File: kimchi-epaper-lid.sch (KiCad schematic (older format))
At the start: 8 parts, among them J1 DF40HC(3.5)-60DS, J2 DF40HC(3.5)-60DS, U1 24C32

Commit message: Partially completed schematics of the lid
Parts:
- added C1, C2, C3, C4, C5, C6, C7, C8, C9: 1uF, symbol Device:C_Small
- added C10, R1, R2: 0.1uF, symbol Device:C_Small
- added IC1: TXS0104ED, SOIC127P600X175-14N, symbol TXS0104ED:TXS0104ED
- added R3, R4: 10k, symbol Device:R_Small_US
- added X1: 52435-2471, symbol epaper-fpc-connector:52435-2471
- renumbered H3 to H2, H2 to H3
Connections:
- net ECSPI1_MOSI: now also X1.14 (D1_Data)
- net ECSPI1_SCLK: now also X1.13 (D0_Clock)
- net ECSPI1_SS0: now also X1.12 (CS)
- net GND: now also C1.2, C10.1, C2.1, C3.1, C4.2, C5.2, C6.2, C7.1, C8.2, C9.1, IC1.7 (GND), R1.1, R2.1, R3.2, R4.2, X1.17 (VSS), X1.8 (BS1)
- net VDD_1V8: now also IC1.1 (VCCA), R1.2
- net VDD_3V3: now also IC1.14 (VCCB), R2.2
- new net: IC1.8 (OE), R3.1
- new net: C3.2, X1.18 (VDD)
- new net: C4.1, X1.19 (VPP)
- new net: C5.1, X1.20 (VSH)
- new net: C6.1, X1.22 (VSL)
- new net: C7.2, X1.24 (VCOM)
- new net: C8.1, X1.4 (VGL)
- new net: C9.2, X1.5 (VGH)
- new net +3V3: C10.2, X1.15 (VDDIO), X1.16 (VCI)
- new net GDR: R4.1, X1.2 (GDR)
- new net LC_BUSY: IC1.13 (B1), X1.9 (BUSY)
- new net LC_DC: IC1.11 (B3), X1.11 (D/C)
- new net LC_RST: IC1.12 (B2), X1.10 (RST)
- new net PREVGH: C1.1, X1.21 (PREVGH)
- new net PREVGL: C2.2, X1.23 (PREVGL)
- new net RESE: X1.3 (RESE)
- no-connect marks 0 -> 7
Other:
- note added: "EINK Display Section"
- note added: "Level Convertor\n"
- note added: "Place close to the connector\n"

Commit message: prouting a few components and updated position
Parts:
- removed IC1: TXS0104ED, SOIC127P600X175-14N, symbol TXS0104ED:TXS0104ED
- removed R1, R2: 0.1uF, symbol Device:C_Small
- removed R3: 10k, symbol Device:R_Small_US
- added C1: 2.2uF, Capacitor_SMD:C_0603_1608Metric, symbol Device:C_Small
- added C2: 1uF, Capacitor_SMD:C_0603_1608Metric, symbol Device:C_Small
- added D1, D2, D3: MBR0530T3G, Diode_SMD:D_SOD-123, symbol Diode:MBR0530
- added L1: 68uH, NLV32T-680J-EF:INDM3225X240N, symbol Device:L_Core_Iron
- added Q1: SI1308EDL-T1-BE3, SI1308EDL-T1-BE3:SOT65P210X110-3N, symbol SI1308EDL-T1-BE3:SI1308EDL-T1-BE3
- added R2: 2.2k, Resistor_SMD:R_0603_1608Metric, symbol Device:R_Small_US
- C10: renamed from C8; footprint (none) -> Capacitor_SMD:C_0603_1608Metric
- C11: renamed from C9; footprint (none) -> Capacitor_SMD:C_0603_1608Metric
- C12: renamed from C10; footprint (none) -> Capacitor_SMD:C_0603_1608Metric
- C3: renamed from C1; footprint (none) -> Capacitor_SMD:C_0603_1608Metric
- C4: renamed from C2; footprint (none) -> Capacitor_SMD:C_0603_1608Metric
- C5: renamed from C3; footprint (none) -> Capacitor_SMD:C_0603_1608Metric
- C6: renamed from C4; footprint (none) -> Capacitor_SMD:C_0603_1608Metric
- C7: renamed from C5; footprint (none) -> Capacitor_SMD:C_0603_1608Metric
- C8: renamed from C6; footprint (none) -> Capacitor_SMD:C_0603_1608Metric
- C9: renamed from C7; footprint (none) -> Capacitor_SMD:C_0603_1608Metric
- R1: renamed from R4; footprint (none) -> Resistor_SMD:R_0603_1608Metric
- X1: footprint (none) -> epaper-fpc-connector:MOLEX_52435-2471
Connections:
- net +3V3 is gone; now on net VDD_3V3: C12.2, X1.15 (VDDIO), X1.16 (VCI)
- net LC_BUSY is gone; now on net SAI3_MCLK: X1.9 (BUSY)
- net LC_DC is gone; now on net SAI3_RXC: X1.11 (D/C)
- net LC_RST is gone; now on net SAI3_TXFS: X1.10 (RST)
- net GDR: now also Q1.1
- net GND: now also C1.2, D1.1 (K), R2.2
- net PREVGH: now also D3.1 (K)
- net PREVGL: now also D2.2 (A)
- net RESE: now also Q1.3, R2.1
- net VDD_3V3: now also C1.1, L1.1
- new net: C2.1, D1.2 (A), D2.1 (K)
- new net: C2.2, D3.2 (A), L1.2, Q1.2
- no-connect marks 7 -> 3
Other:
- note removed: "Level Convertor\n"
- moved on the sheet: C10, C11, C12, C3, C4, C5, C6, C7, C8, C9, R1, X1

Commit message: Fixed issues with routing
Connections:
- net USB2_DN is gone; now on net PCIE_USB_D_N: J1.59 (Pin_59)
- net USB2_DP is gone; now on net PCIE_USB_D_P: J1.60 (Pin_60)
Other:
- note added: "Connected these together, so that USB2 pins \nwill be accessible on the PCIE port, as they \nare not being used."
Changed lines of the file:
@@
 	1    0    0    -1
 $EndComp
+Text GLabel 12010 2540 3    50   Input ~ 0
+PCIE_USB_D_N
+Text GLabel 12430 2540 3    50   Input ~ 0
+PCIE_USB_D_P
+Text GLabel 12430 1935 1    50   Input ~ 0
+USB2_DP
+Text GLabel 12010 1940 1    50   Input ~ 0
+USB2_DN
+Wire Wire Line
+	12010 2540 12010 1940
+Wire Wire Line
+	12430 1935 12430 2540
+Text Notes 12565 2435 0    79   ~ 0
+Connected these together, so that USB2 pins \nwill be accessible on the PCIE port, as they \nare not being used.
 $EndSCHEMATC

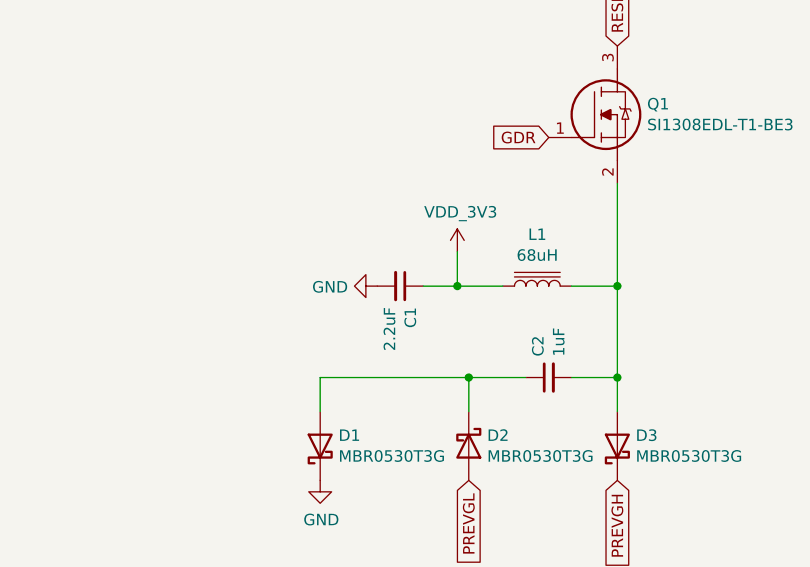
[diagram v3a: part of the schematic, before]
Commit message: Replaced inductor and completed routing (acq review)
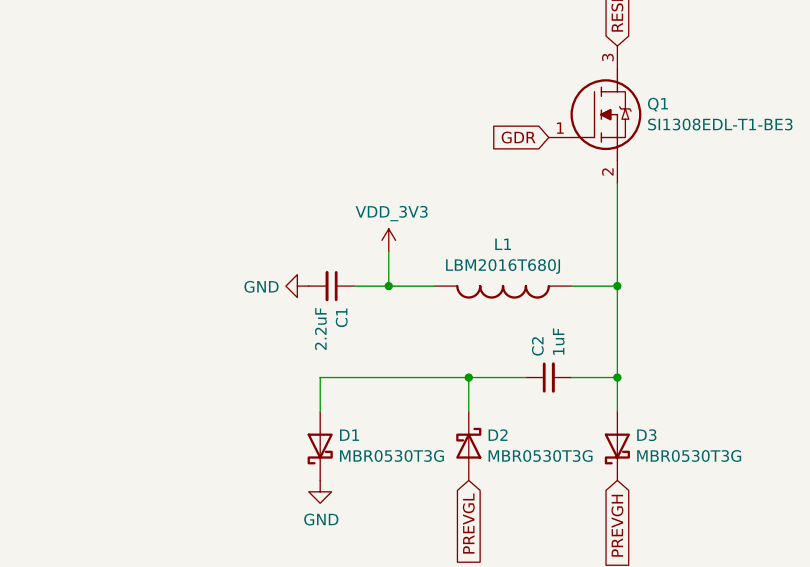
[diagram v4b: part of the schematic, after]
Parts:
- removed L1: 68uH, NLV32T-680J-EF:INDM3225X240N, symbol Device:L_Core_Iron
- added L1: LBM2016T680J, LBM2016T680J:INDC2016X180N, symbol LBM2016T680J:LBM2016T680J
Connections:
- net VDD_3V3: now also L1.1
- net at C2.2, D3.2 (A), Q1.2: now also L1.2
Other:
- moved on the sheet: C1
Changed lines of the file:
@@
 L Device:C_Small C1
 U 1 1 6029C582
-P 4400 7700
-F 0 "C1" H 4308 7746 50  0000 R CNN
-F 1 "2.2uF" H 4308 7655 50  0000 R CNN
-F 2 "Capacitor_SMD:C_0603_1608Metric" H 4400 7700 50  0001 C CNN
-F 3 "~" H 4400 7700 50  0001 C CNN
-	1    4400 7700
+P 4100 7700
+F 0 "C1" H 4008 7746 50  0000 R CNN
+F 1 "2.2uF" H 4008 7655 50  0000 R CNN
+F 2 "Capacitor_SMD:C_0603_1608Metric" H 4100 7700 50  0001 C CNN
+F 3 "~" H 4100 7700 50  0001 C CNN
+	1    4100 7700
 	0    1    -1   0
 $EndComp
@@
 	1    5050 8100
 	0    -1   1    0
-$EndComp
-$Comp
-L Device:L_Core_Iron L1
-U 1 1 6029F5E3
-P 5000 7700
-F 0 "L1" V 5225 7700 50  0000 C CNN
-F 1 "68uH" V 5134 7700 50  0000 C CNN
-F 2 "NLV32T-680J-EF:INDM3225X240N" H 5000 7700 50  0001 C CNN
-F 3 "~" H 5000 7700 50  0001 C CNN
-	1    5000 7700
-	0    -1   -1   0
 $EndComp
 $Comp
@@
 	5350 7700 5350 8100
 Wire Wire Line
-	4850 7700 4650 7700
+	4550 7700 4350 7700
 $Comp
 L power:GND #PWR06
 U 1 1 60330ACC
-P 4300 7700
-F 0 "#PWR06" H 4300 7450 50  0001 C CNN
-F 1 "GND" V 4305 7572 50  0000 R CNN
-F 2 "" H 4300 7700 50  0001 C CNN
-F 3 "" H 4300 7700 50  0001 C CNN
-	1    4300 7700
+P 4000 7700
+F 0 "#PWR06" H 4000 7450 50  0001 C CNN
+F 1 "GND" V 4005 7572 50  0000 R CNN
+F 2 "" H 4000 7700 50  0001 C CNN
+F 3 "" H 4000 7700 50  0001 C CNN
+	1    4000 7700
 	0    1    1    0
 $EndComp
 Wire Wire Line
-	4650 7550 4650 7700
-Connection ~ 4650 7700
+	4350 7550 4350 7700
+Connection ~ 4350 7700
 Wire Wire Line
-	4650 7700 4500 7700
+	4350 7700 4200 7700
 $Comp
 L power:GND #PWR05
@@
 RESE
 $Comp
-L kimchi_ulid:VDD_3V3 #PWR?
+L kimchi_ulid:VDD_3V3 #PWR014
 U 1 1 6048F43C
 P 9850 7600
-F 0 "#PWR?" H 9850 7450 50  0001 C CNN
+F 0 "#PWR014" H 9850 7450 50  0001 C CNN
 F 1 "VDD_3V3" V 9865 7727 50  0000 L CNN
 F 2 "" H 9850 7600 50  0001 C CNN
@@
 $EndComp
 $Comp
-L kimchi_ulid:VDD_3V3 #PWR?
+L kimchi_ulid:VDD_3V3 #PWR07
 U 1 1 604938CB
-P 4650 7550
-F 0 "#PWR?" H 4650 7400 50  0001 C CNN
-F 1 "VDD_3V3" H 4665 7723 50  0000 C CNN
-F 2 "" H 4650 7550 50  0001 C CNN
-F 3 "" H 4650 7550 50  0001 C CNN
-	1    4650 7550
+P 4350 7550
+F 0 "#PWR07" H 4350 7400 50  0001 C CNN
+F 1 "VDD_3V3" H 4365 7723 50  0000 C CNN
+F 2 "" H 4350 7550 50  0001 C CNN
+F 3 "" H 4350 7550 50  0001 C CNN
+	1    4350 7550
 	1    0    0    -1
 $EndComp
@@
 Text Notes 12565 2435 0    79   ~ 0
 Connected these together, so that USB2 pins \nwill be accessible on the PCIE port, as they \nare not being used.
+$Comp
+L LBM2016T680J:LBM2016T680J L1
+U 1 1 6068AC33
+P 4850 7700
+F 0 "L1" H 4850 7881 50  0000 C CNN
+F 1 "LBM2016T680J" H 4850 7790 50  0000 C CNN
+F 2 "LBM2016T680J:INDC2016X180N" H 4850 7700 50  0001 L BNN
+F 3 "" H 4850 7700 50  0001 L BNN
+	1    4850 7700
+	1    0    0    -1
+$EndComp
 $EndSCHEMATC

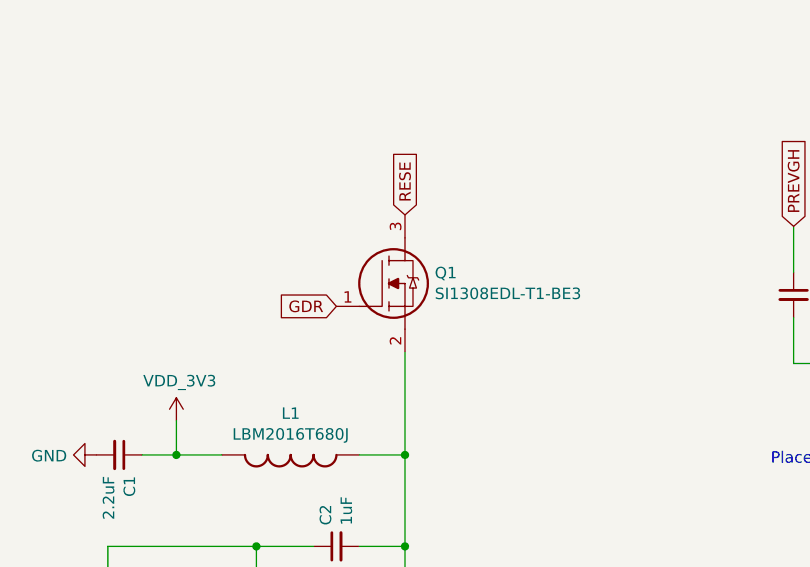
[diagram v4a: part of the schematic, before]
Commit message: Fixed mistake in mosfet schematics
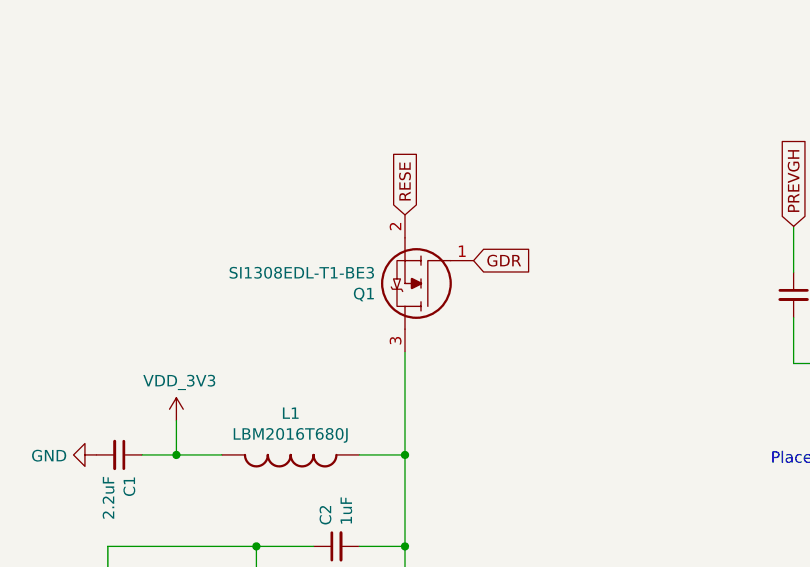
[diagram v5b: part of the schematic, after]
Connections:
- net RESE: now also Q1.2; no longer Q1.3
- net at C2.2, D3.2 (A), L1.2: now also Q1.3; no longer Q1.2
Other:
- moved on the sheet: Q1
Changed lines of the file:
@@
 	0    -1   1    0
-$EndComp
-$Comp
-L SI1308EDL-T1-BE3:SI1308EDL-T1-BE3 Q1
-U 1 1 602E5C48
-P 5050 7050
-F 0 "Q1" H 5480 7196 50  0000 L CNN
-F 1 "SI1308EDL-T1-BE3" H 5480 7105 50  0000 L CNN
-F 2 "SI1308EDL-T1-BE3:SOT65P210X110-3N" H 5500 7000 50  0001 L CNN
-F 3 "https://www.mouser.es/datasheet/2/427/si1308edl-1764588.pdf" H 5500 6900 50  0001 L CNN
-F 4 "MOSFET 30V N-CHANNEL (D-S)" H 5500 6800 50  0001 L CNN "Description"
-F 5 "1.1" H 5500 6700 50  0001 L CNN "Height"
-F 6 "Vishay" H 5500 6600 50  0001 L CNN "Manufacturer_Name"
-F 7 "SI1308EDL-T1-BE3" H 5500 6500 50  0001 L CNN "Manufacturer_Part_Number"
-F 8 "78-SI1308EDL-T1-BE3" H 5500 6400 50  0001 L CNN "Mouser Part Number"
-F 9 "https://www.mouser.co.uk/ProductDetail/Vishay-Siliconix/SI1308EDL-T1-BE3/?qs=zW32dvEIR3shhEGZ2ACCcQ%3D%3D" H 5500 6300 50  0001 L CNN "Mouser Price/Stock"
-F 10 "" H 5500 6200 50  0001 L CNN "Arrow Part Number"
-F 11 "" H 5500 6100 50  0001 L CNN "Arrow Price/Stock"
-	1    5050 7050
-	1    0    0    -1
 $EndComp
 Wire Wire Line
@@
 Text GLabel 5350 8550 3    50   Input ~ 0
 PREVGH
-Text GLabel 5050 7050 0    50   Input ~ 0
+Text GLabel 5650 6850 2    50   Input ~ 0
 GDR
 Text GLabel 5350 6650 1    50   Input ~ 0
@@
 	1    0    0    -1
 $EndComp
+$Comp
+L SI1308EDL-T1-BE3:SI1308EDL-T1-BE3 Q1
+U 1 1 602E5C48
+P 5650 6850
+F 0 "Q1" H 6080 6996 50  0000 L CNN
+F 1 "SI1308EDL-T1-BE3" H 6080 6905 50  0000 L CNN
+F 2 "SI1308EDL-T1-BE3:SOT65P210X110-3N" H 6100 6800 50  0001 L CNN
+F 3 "https://www.mouser.es/datasheet/2/427/si1308edl-1764588.pdf" H 6100 6700 50  0001 L CNN
+F 4 "MOSFET 30V N-CHANNEL (D-S)" H 6100 6600 50  0001 L CNN "Description"
+F 5 "1.1" H 6100 6500 50  0001 L CNN "Height"
+F 6 "Vishay" H 6100 6400 50  0001 L CNN "Manufacturer_Name"
+F 7 "SI1308EDL-T1-BE3" H 6100 6300 50  0001 L CNN "Manufacturer_Part_Number"
+F 8 "78-SI1308EDL-T1-BE3" H 6100 6200 50  0001 L CNN "Mouser Part Number"
+F 9 "https://www.mouser.co.uk/ProductDetail/Vishay-Siliconix/SI1308EDL-T1-BE3/?qs=zW32dvEIR3shhEGZ2ACCcQ%3D%3D" H 6100 6100 50  0001 L CNN "Mouser Price/Stock"
+F 10 "" H 6100 6000 50  0001 L CNN "Arrow Part Number"
+F 11 "" H 6100 5900 50  0001 L CNN "Arrow Price/Stock"
+	1    5650 6850
+	-1   0    0    1
+$EndComp
 $EndSCHEMATC
